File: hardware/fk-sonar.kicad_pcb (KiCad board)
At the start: 2 copper layers, 34.5 x 70.4 mm, 79 parts, among them J1 CONN_01x03, J10 CONN_01x02, J2 CONN_02x05_SWD, J3 RF-SMA-EDGE, J4 MICRO-USB, J5 S2B-PH-SM4-TB, J6 CONN_01x04, J7 S2B-PH-SM4-TB, J8 CONN_01x03_SERIAL, J9 CONN_01x05, M1 MOUNT_HOLE, M3 MOUNT_HOLE, M4 MOUNT_HOLE, M6 MOUNT_HOLE, Q1 2N7002LT1G, SW1 SPNO, U1 ATSAMD21G18A-AU, U2 RFM95W, U3 BQ24074RGTT, U4 S25FL116K0XMFI041, U5 MAX1704XX, U6 MCP1700T-3302E/MB, U7 SK6812, U8 TPS2051B, Y1 FC-135

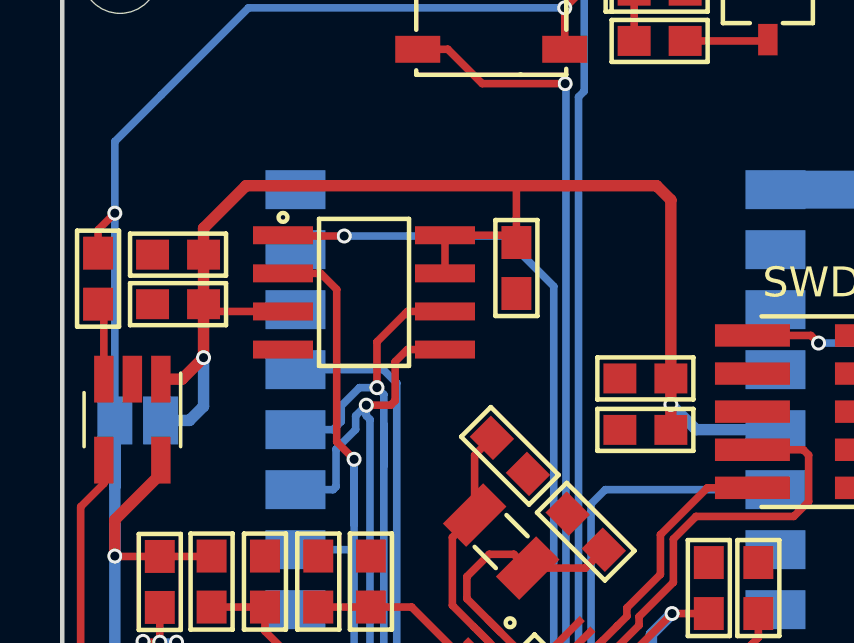
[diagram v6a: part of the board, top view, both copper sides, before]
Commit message: Use more compatible FP for flash.
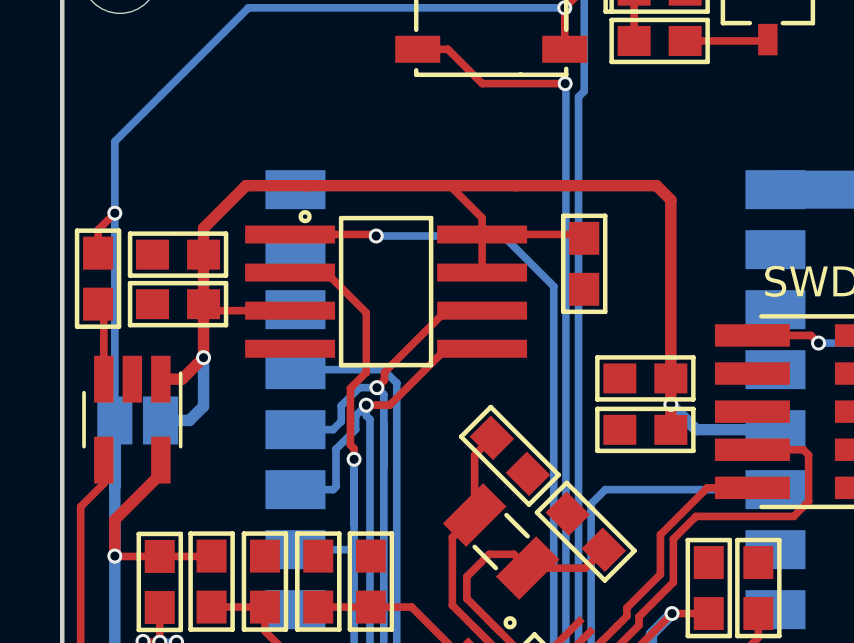
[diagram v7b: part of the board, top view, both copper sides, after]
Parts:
- U4: footprint conservify:SOIC-8-N -> conservify:SOIC-8-N-WIDE
- moved C20 2.26 mm to (139.6, 74.1)
- moved U4 0.74 mm to (133.0, 75.0)
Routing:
- net /PERIPH_3V3: track 45.5 -> 52.0 mm
- net /SCK: track 29.7 -> 30.2 mm

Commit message: Bump version and plot gerbers.
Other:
- board text added: "v0.6"
- board text removed: "v0.5"
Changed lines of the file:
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@@
   (gr_arc (start 155.702 63.246) (end 155.702 62.23) (angle 90) (layer Edge.Cuts) (width 0.15))
   (gr_arc (start 155.702 131.572) (end 156.718 131.572) (angle 90) (layer Edge.Cuts) (width 0.15))
-  (gr_text v0.5 (at 155.4734 127.2794 90) (layer F.SilkS)
+  (gr_text v0.6 (at 155.4734 127.2794 90) (layer F.SilkS)
     (effects (font (size 1 1) (thickness 0.2)))
   )
